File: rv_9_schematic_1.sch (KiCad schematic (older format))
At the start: 10 parts

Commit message: Working on trim system
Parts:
- added F?: Fuse, symbol Fuse
- added F? (x3): 1A, symbol Fuse
- added G? (x3): LCL, symbol LCL
- added S? (x2): RayAllenServo, symbol RayAllenServo
- added S? (x2): LEDPOSITION_INDICATOR, symbol LEDPOSITION_INDICATOR
- added SW?: Instrument Light, symbol SW_SPST
- added T?: TrimRelay, symbol TrimRelay
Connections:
- net at SWP4.2 (B): now also SWC4.2 (B), T?.3 (Ail_Up_In)
- net at SWP2.2 (B): now also SWC2.2 (B), T?.4 (Ail_Dn_In)
- net at SWP3.2 (B): now also SWC3.2 (B), T?.1 (Elev_Up_In)
- net at SWP1.2 (B): now also SWC1.2 (B), T?.2 (Elev_Dn_In)
- new net: S?.1 (WHITE), T?.5 (Elev_Up_Out)
- new net: S?.2 (WHITE), T?.6 (Elev_Dn_Out)
- new net: S?.1 (ORANGE), S?.3 (ORANGE) (x2)
- new net: S?.2 (GREEN), S?.4 (GREEN) (x2)
- new net: S?.3 (BLUE), S?.5 (BLUE) (x2)
- new net: S?.1 (WHITE), T?.7 (Ail_Up_Out)
- new net: S?.2 (WHITE), T?.8 (Ail_Dn_Out)
- new net: F?.2, S?.4 (RED)
- new net: G?.1, S?.5 (BLACK) (x2)
- new net: S?.6 (WHITE), S?.6 (WHITE), SW?.2 (B)
- new net: F?.2, SW?.1 (A)
- new net: F?.2, T?.10 (PWR-AIL)
- new net: G?.1, T?.12 (Gnd)
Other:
- note added: "Copilot Stick Grip"
- note added: "Pilot Stick Grip"

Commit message: Many updates
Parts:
- removed F?: 1A, symbol Fuse
- removed G? (x3): LCL, symbol LCL
- added B?: Endurance-Bus, symbol BUS-BAR
- added B?: Main-Bus, symbol BUS-BAR
- added G? (x5): PNL, symbol LCL
- added J1, J2: Mini-DIN-6, symbol Mini-DIN-6
- S1: renamed from S?; value RayAllenServo -> Elevator Trim Servo
- S2: renamed from S?; value RayAllenServo -> Aileron Trim Servo
- S3: renamed from S?; value LEDPOSITION_INDICATOR -> Aileron Trim Indicator
- S4: renamed from S?; value LEDPOSITION_INDICATOR -> Elevator Trim Indicator
- gave numbers to parts that had none: 1
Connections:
- net at SWP4.2 (B), T1.3 (Ail_Up_In): now also J2.5; no longer SWC4.2 (B)
- net at SWP2.2 (B), T1.4 (Ail_Dn_In): now also J2.3; no longer SWC2.2 (B)
- net at SWP3.2 (B), T1.1 (Elev_Up_In): now also J2.4; no longer SWC3.2 (B)
- net at SWP1.2 (B), T1.2 (Elev_Dn_In): now also J2.2; no longer SWC1.2 (B)
- net at SWC5.2 (B): now also J1.1
- net at S4.4 (RED): now also F?.1, T1.11 (PWR-EL); no longer F?.2
- net at S4.5 (BLACK): now also G?.1
- net at T1.10 (PWR-AIL): now also F?.1, S3.4 (RED)
- net at T1.12 (Gnd): now also G?.1
- net at S3.5 (BLACK): now also G?.1
- net GND: no longer names the net of SWP1.3 (C), SWP2.3 (C), SWP3.3 (C), SWP4.3 (C), SWP5.3 (C)
- net GND: now also G?.1; no longer SWC1.3 (C), SWC2.3 (C), SWC3.3 (C), SWC4.3 (C), SWC5.3 (C)
- new net: J1.5, SWC4.2 (B)
- new net: J1.6, SWC1.3 (C), SWC2.3 (C), SWC3.3 (C), SWC4.3 (C), SWC5.3 (C)
- new net: J1.3, SWC2.2 (B)
- new net: J1.4, SWC3.2 (B)
- new net: J1.2, SWC1.2 (B)
- new net: G?.1, J2.6
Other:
- note added: "Aileron\nTrim"
- note added: "Cabin"
- note added: "Elevator\nTrim"
- note added: "Instrument\nLights"
- note added: "Panel"
- moved on the sheet: F?, S1, S2, SW?

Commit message: Added lighting systems
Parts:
- added G?: LCL, symbol LCL
- added SW?: Flap Down, symbol SW_SPST
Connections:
- net at T1.9 (Flap_Dn): now also SW?.2 (B)
- new net: G?.1, SW?.1 (A)
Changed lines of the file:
@@
 EESchema Schematic File Version 2
-LIBS:rv_9_schematic-rescue
 LIBS:power
 LIBS:device
@@
 Text Notes 1950 3800 0    60   ~ 0
 PTT
-Text HLabel 1225 7750 0    60   Input ~ 0
-12V
 Wire Wire Line
 	2650 1600 2850 1600
@@
 Connection ~ 2850 2150
 Wire Wire Line
-	2650 2750 2850 2750
+	2850 2750 2650 2750
 Connection ~ 2850 2750
 Wire Wire Line
-	2650 3350 2850 3350
+	2850 3350 2650 3350
 Connection ~ 2850 3350
 Wire Wire Line
@@
 	3525 1250 5200 1250
 Wire Wire Line
-	5200 1250 5200 1600
-Wire Wire Line
-	5200 1600 5200 2150
-Wire Wire Line
-	5200 2150 5200 2750
-Wire Wire Line
-	5200 2750 5200 3350
-Wire Wire Line
-	5200 3350 5200 3950
+	5200 1250 5200 3950
 Wire Wire Line
 	5000 1600 5200 1600
@@
 	1575 5900 1575 6150
 Wire Wire Line
-	1975 5775 1975 6150
-Wire Wire Line
-	1975 6150 1975 6450
+	1975 5775 1975 6450
 Connection ~ 1975 6150
 $Comp
@@
 Wire Wire Line
 	3175 4500 3550 4500
-Text HLabel 950  5500 0    60   Input ~ 0
-12V
 Wire Notes Line
 	9225 2750 9225 3750
@@
 Connection ~ 2850 3950
 Wire Wire Line
-	2850 1600 2850 2150
-Wire Wire Line
-	2850 2150 2850 2750
-Wire Wire Line
-	2850 2750 2850 3350
-Wire Wire Line
-	2850 3350 2850 3950
-Wire Wire Line
-	2850 3950 2850 5425
+	2850 1600 2850 5425
 $Comp
 L LCL G?
@@
 Text Notes 975  5825 0    60   ~ 0
 Instrument\nLights
+$Comp
+L SW_SPST SW?
+U 1 1 5B6739D6
+P 6225 3400
+F 0 "SW?" H 6225 3525 50  0000 C CNN
+F 1 "Flap Down" H 6225 3300 50  0000 C CNN
+F 2 "" H 6225 3400 50  0001 C CNN
+F 3 "" H 6225 3400 50  0001 C CNN
+	1    6225 3400
+	1    0    0    -1
+$EndComp
+$Comp
+L LCL G?
+U 1 1 5B673BCE
+P 5800 3925
+F 0 "G?" H 5875 4050 60  0000 C CNN
+F 1 "LCL" H 5800 3800 60  0000 C CNN
+F 2 "" H 5800 3925 60  0001 C CNN
+F 3 "" H 5800 3925 60  0001 C CNN
+	1    5800 3925
+	1    0    0    -1
+$EndComp
+Wire Wire Line
+	5800 3650 5800 3400
+Wire Wire Line
+	5800 3400 6025 3400
+Wire Wire Line
+	7000 4075 6525 4075
+Wire Wire Line
+	6525 4075 6525 3400
+Wire Wire Line
+	6525 3400 6425 3400
 $EndSCHEMATC

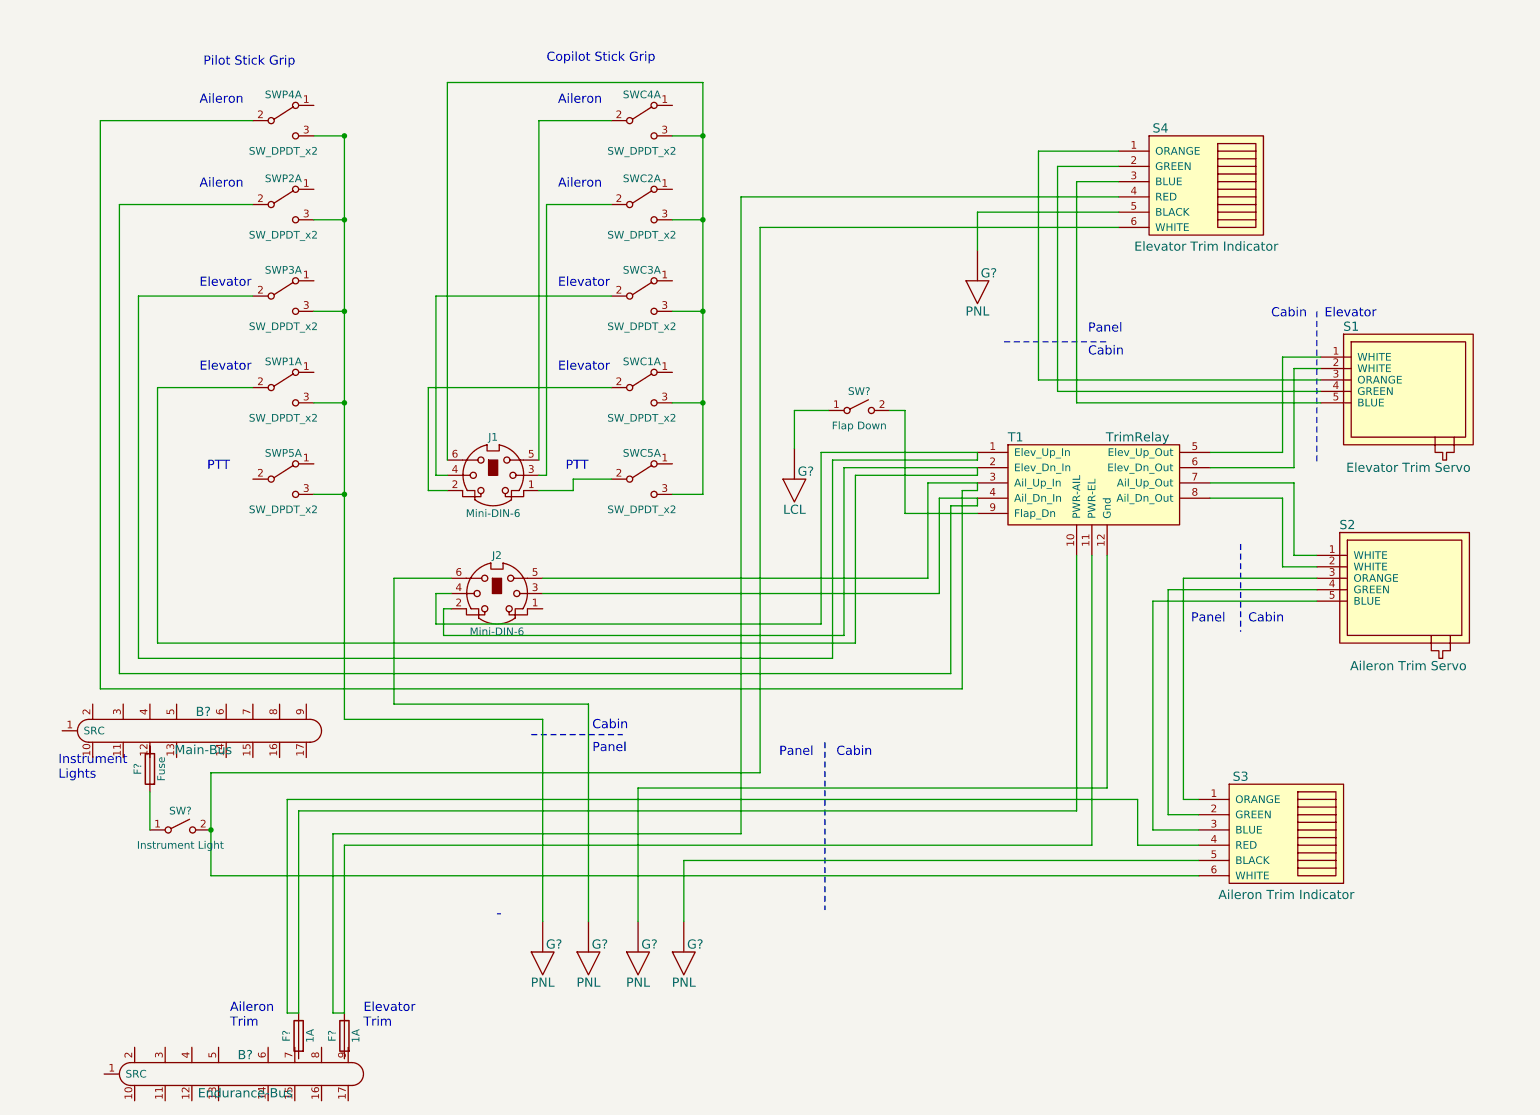
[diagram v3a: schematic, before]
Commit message: Added sheets 3,4,5
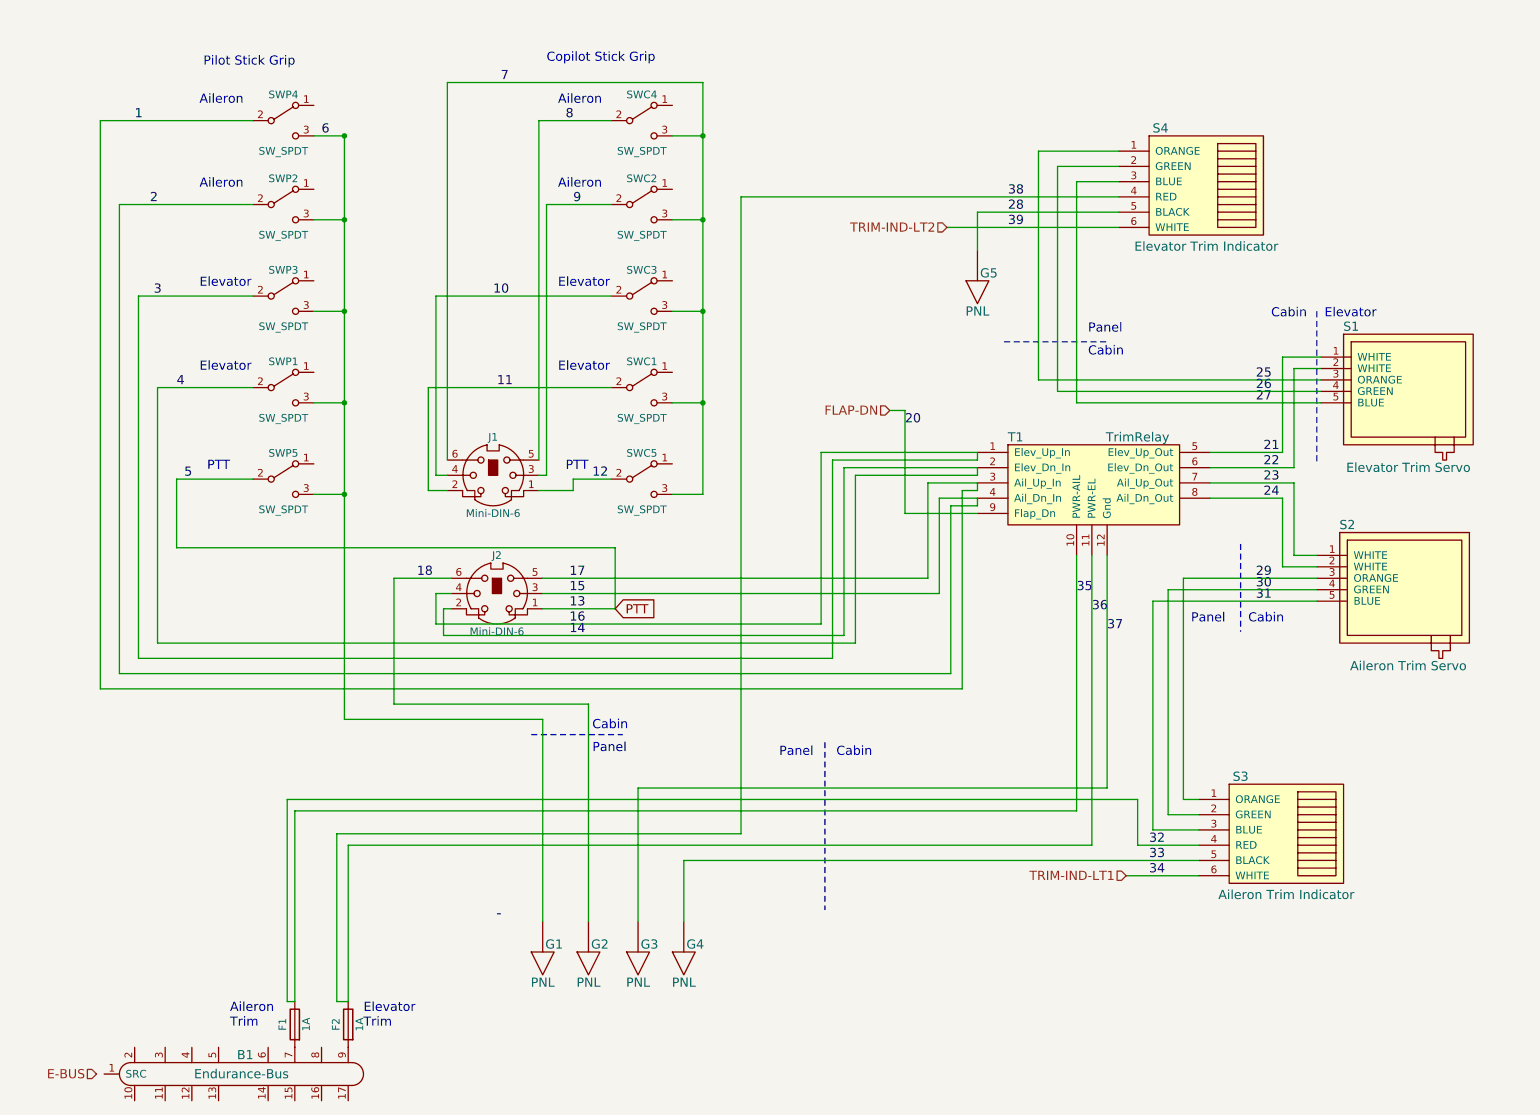
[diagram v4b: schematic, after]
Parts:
- removed B?: Main-Bus, symbol BUS-BAR
- removed F?: Fuse, symbol Fuse
- removed G?: LCL, symbol LCL
- removed SW?: Instrument Light, symbol SW_SPST
- removed SW?: Flap Down, symbol SW_SPST
- removed SWC1, SWC2, SWC3, SWC4, SWC5, SWP1, SWP2, SWP3, SWP4, SWP5: SW_DPDT_x2, symbol SW_DPDT_x2
- added SWC1, SWC2, SWC3, SWC4, SWC5, SWP1, SWP2, SWP3, SWP4, SWP5: SW_SPDT, symbol SW_SPDT
- gave numbers to parts that had none: 8
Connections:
- net 1: now reaches J2.5, T1.3 (Ail_Up_In)
- net 1: now also SWP4.2 (B)
- net 6: now reaches G1.1
- net 6: now also SWP1.3 (C), SWP2.3 (C), SWP3.3 (C), SWP4.3 (C), SWP5.3 (C)
- net 15: now reaches J2.3, T1.4 (Ail_Dn_In)
- net 15: now also SWP2.2 (B)
- net 16: now reaches J2.4, T1.1 (Elev_Up_In)
- net 16: now also SWP3.2 (B)
- net 14: now reaches J2.2, T1.2 (Elev_Dn_In)
- net 14: now also SWP1.2 (B)
- net 8: now reaches J1.5
- net 8: now also SWC4.2 (B)
- net 7: now reaches J1.6
- net 7: now also SWC1.3 (C), SWC2.3 (C), SWC3.3 (C), SWC4.3 (C), SWC5.3 (C)
- net 9: now reaches J1.3
- net 9: now also SWC2.2 (B)
- net 10: now reaches J1.4
- net 10: now also SWC3.2 (B)
- net 11: now reaches J1.2
- net 11: now also SWC1.2 (B)
- net 12: now reaches J1.1
- net 12: now also SWC5.2 (B)
- net 21: now reaches S1.1 (WHITE), T1.5 (Elev_Up_Out)
- net 22: now reaches S1.2 (WHITE), T1.6 (Elev_Dn_Out)
- net 25: now reaches S1.3 (ORANGE), S4.1 (ORANGE)
- net 26: now reaches S1.4 (GREEN), S4.2 (GREEN)
- net 27: now reaches S1.5 (BLUE), S4.3 (BLUE)
- net 23: now reaches S2.1 (WHITE), T1.7 (Ail_Up_Out)
- net 24: now reaches S2.2 (WHITE), T1.8 (Ail_Dn_Out)
- net 29: now reaches S2.3 (ORANGE), S3.1 (ORANGE)
- net 30: now reaches S2.4 (GREEN), S3.2 (GREEN)
- net 31: now reaches S2.5 (BLUE), S3.3 (BLUE)
- net 36: now reaches F2.1, S4.4 (RED), T1.11 (PWR-EL)
- net 28: now reaches G5.1, S4.5 (BLACK)
- net TRIM-IND-LT1: now reaches S3.6 (WHITE)
- net TRIM-IND-LT1: no longer S4.6 (WHITE)
- net 32: now reaches F1.1, S3.4 (RED), T1.10 (PWR-AIL)
- net 37: now reaches G3.1, T1.12 (Gnd)
- net FLAP-DN: now reaches T1.9 (Flap_Dn)
- net 33: now reaches G4.1, S3.5 (BLACK)
- net at F1.2: now also B1.7
- net at F2.2: now also B1.9
- net PTT: now reaches J2.1
- net PTT: now also SWP5.2 (B)
- net 18: now reaches G2.1, J2.6
- new net TRIM-IND-LT2: S4.6 (WHITE)
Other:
- note removed: "Instrument\nLights"
- moved on the sheet: F1, F2

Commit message: new version kicad changes
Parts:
- B1: symbol BUS-BAR -> AvionicSchematic:BUS-BAR
- F1, F2: symbol Fuse -> rv_9_schematic-rescue:Fuse
- G1, G2, G3, G4, G5: symbol LCL -> AvionicSchematic:LCL
- J1, J2: symbol Mini-DIN-6 -> rv_9_schematic-rescue:Mini-DIN-6
- S1, S2: symbol RayAllenServo -> AvionicSchematic:RayAllenServo
- S3, S4: symbol LEDPOSITION_INDICATOR -> AvionicSchematic:LEDPOSITION_INDICATOR
- SWC1, SWC2, SWC3, SWC4, SWC5, SWP1, SWP2, SWP3, SWP4, SWP5: symbol SW_SPDT -> rv_9_schematic-rescue:SW_SPDT
- T1: symbol TrimRelay -> AvionicSchematic:TrimRelay
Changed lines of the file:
@@
-EESchema Schematic File Version 2
-LIBS:power
-LIBS:device
-LIBS:switches
-LIBS:relays
-LIBS:motors
-LIBS:transistors
-LIBS:conn
-LIBS:linear
-LIBS:regul
-LIBS:74xx
-LIBS:cmos4000
-LIBS:adc-dac
-LIBS:memory
-LIBS:xilinx
-LIBS:microcontrollers
-LIBS:dsp
-LIBS:microchip
-LIBS:analog_switches
-LIBS:motorola
-LIBS:texas
-LIBS:intel
-LIBS:audio
-LIBS:interface
-LIBS:digital-audio
-LIBS:philips
-LIBS:display
-LIBS:cypress
-LIBS:siliconi
-LIBS:opto
-LIBS:atmel
-LIBS:contrib
-LIBS:valves
-LIBS:AvionicSchematic
-LIBS:rv_9_schematic-cache
-EELAYER 25 0
+EESchema Schematic File Version 4
+EELAYER 30 0
 EELAYER END
 $Descr USLetter 11000 8500
@@
 Wire Wire Line
 	2650 1600 2850 1600
-Connection ~ 2850 1600
 Wire Wire Line
 	2650 2150 2850 2150
@@
 	3525 1250 5200 1250
 Wire Wire Line
-	5200 1250 5200 3950
+	5200 1250 5200 1600
 Wire Wire Line
 	5000 1600 5200 1600
@@
 	5200 3950 5000 3950
 $Comp
-L RayAllenServo S1
+L AvionicSchematic:RayAllenServo S1
 U 1 1 5B6530DF
 P 9825 3250
@@
 $EndComp
 $Comp
-L RayAllenServo S2
+L AvionicSchematic:RayAllenServo S2
 U 1 1 5B65324A
 P 9800 4550
@@
 $EndComp
 $Comp
-L LEDPOSITION_INDICATOR S4
+L AvionicSchematic:LEDPOSITION_INDICATOR S4
 U 1 1 5B6532A0
 P 8400 1925
@@
 $EndComp
 $Comp
-L TrimRelay T1
+L AvionicSchematic:TrimRelay T1
 U 1 1 5B6556F7
 P 7750 3850
@@
 	7000 3925 7000 3875
 $Comp
-L LEDPOSITION_INDICATOR S3
+L AvionicSchematic:LEDPOSITION_INDICATOR S3
 U 1 1 5B658112
 P 8925 6175
@@
 	6800 2200 7925 2200
 $Comp
-L Fuse F1
+L rv_9_schematic-rescue:Fuse F1
 U 1 1 5B65A0B7
 P 2525 7425
+AR Path="/5B65A0B7" Ref="F1"  Part="1"
+AR Path="/5B61469B/5B65A0B7" Ref="F1"  Part="1"
 F 0 "F1" V 2605 7425 50  0000 C CNN
 F 1 "1A" V 2450 7425 50  0000 C CNN
@@
 	7650 4350 7650 6025
 $Comp
-L Fuse F2
+L rv_9_schematic-rescue:Fuse F2
 U 1 1 5B65B860
 P 2875 7425
+AR Path="/5B65B860" Ref="F2"  Part="1"
+AR Path="/5B61469B/5B65B860" Ref="F2"  Part="1"
 F 0 "F2" V 2955 7425 50  0000 C CNN
 F 1 "1A" V 2800 7425 50  0000 C CNN
@@
 Copilot Stick Grip
 $Comp
-L BUS-BAR B1
+L AvionicSchematic:BUS-BAR B1
 U 1 1 5B666EE4
 P 2200 7750
@@
 	5075 6350 5075 6750
 $Comp
-L LCL G5
+L AvionicSchematic:LCL G5
 U 1 1 5B66F567
 P 7000 2625
@@
 $EndComp
 $Comp
-L LCL G3
+L AvionicSchematic:LCL G3
 U 1 1 5B66F920
 P 4775 7025
@@
 $EndComp
 $Comp
-L LCL G4
+L AvionicSchematic:LCL G4
 U 1 1 5B66FD52
 P 5075 7025
@@
 	2875 7275 2875 6250
 $Comp
-L Mini-DIN-6 J2
+L rv_9_schematic-rescue:Mini-DIN-6 J2
 U 1 1 5B672BF9
 P 3850 4600
@@
 $EndComp
 $Comp
-L Mini-DIN-6 J1
+L rv_9_schematic-rescue:Mini-DIN-6 J1
 U 1 1 5B672CE7
 P 3825 3825
@@
 	4350 3925 4125 3925
 $Comp
-L LCL G2
+L AvionicSchematic:LCL G2
 U 1 1 5B6771A7
 P 4450 7025
@@
 Connection ~ 2850 3950
 Wire Wire Line
-	2850 1600 2850 5425
-$Comp
-L LCL G1
+	2850 1600 2850 2150
+$Comp
+L AvionicSchematic:LCL G1
 U 1 1 5B68237B
 P 4150 7025
@@
 E-BUS
 $Comp
-L SW_SPDT SWP4
+L rv_9_schematic-rescue:SW_SPDT SWP4
 U 1 1 5B7A73EF
 P 2450 1500
@@
 $EndComp
 $Comp
-L SW_SPDT SWP2
+L rv_9_schematic-rescue:SW_SPDT SWP2
 U 1 1 5B7A88E9
 P 2450 2050
@@
 $EndComp
 $Comp
-L SW_SPDT SWP3
+L rv_9_schematic-rescue:SW_SPDT SWP3
 U 1 1 5B7A9058
 P 2450 2650
@@
 $EndComp
 $Comp
-L SW_SPDT SWP1
+L rv_9_schematic-rescue:SW_SPDT SWP1
 U 1 1 5B7A9635
 P 2450 3250
@@
 $EndComp
 $Comp
-L SW_SPDT SWP5
+L rv_9_schematic-rescue:SW_SPDT SWP5
 U 1 1 5B7A9743
 P 2450 3850
@@
 $EndComp
 $Comp
-L SW_SPDT SWC4
+L rv_9_schematic-rescue:SW_SPDT SWC4
 U 1 1 5B7AA0B6
 P 4800 1500
@@
 $EndComp
 $Comp
-L SW_SPDT SWC2
+L rv_9_schematic-rescue:SW_SPDT SWC2
 U 1 1 5B7AA6AB
 P 4800 2050
@@
 $EndComp
 $Comp
-L SW_SPDT SWC3
+L rv_9_schematic-rescue:SW_SPDT SWC3
 U 1 1 5B7AA78E
 P 4800 2650
@@
 $EndComp
 $Comp
-L SW_SPDT SWC1
+L rv_9_schematic-rescue:SW_SPDT SWC1
 U 1 1 5B7AA872
 P 4800 3250
@@
 $EndComp
 $Comp
-L SW_SPDT SWC5
+L rv_9_schematic-rescue:SW_SPDT SWC5
 U 1 1 5B7AA95B
 P 4800 3850
@@
 Text Label 4325 4700 0    60   ~ 0
 13
+Wire Wire Line
+	2850 2150 2850 2750
+Wire Wire Line
+	2850 2750 2850 3350
+Wire Wire Line
+	2850 3350 2850 3950
+Wire Wire Line
+	5200 1600 5200 2150
+Wire Wire Line
+	5200 2150 5200 2750
+Wire Wire Line
+	5200 2750 5200 3350
+Wire Wire Line
+	5200 3350 5200 3950
+Wire Wire Line
+	2850 3950 2850 5425
 $EndSCHEMATC
